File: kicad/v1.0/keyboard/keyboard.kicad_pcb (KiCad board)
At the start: 2 copper layers, 162 x 50 mm, 89 parts, among them J1 PMOD, J2 Conn_01x02, J3 Conn_01x02, SW1 @, SW10 I, SW11 J, SW12 K, SW13 L, SW14 M, SW15 N, SW16 O, SW17 P, SW18 Q, SW19 R, SW2 A, SW20 S, SW21 T, SW22 U, SW23 V, SW24 W, SW25 X, SW26 Y, SW27 Z, SW28 0, SW29 1, SW3 B, SW30 2, SW31 3, SW32 4, SW33 5, SW34 6, SW35 7, SW36 0, SW37 1, SW38 2, SW39 3, SW4 C, SW40 4, SW41 5, SW42 6, SW43 7, SW44 8, SW45 9, SW46 ., SW47 8, SW48 9, SW49 :, SW5 D, SW50 ;, SW51 ,, SW52 -, SW53 ., SW54 /, SW55 ENTER, SW56 ENTER, SW57 CLEAR, SW58 BREAK, SW59 UP, SW6 E, SW60 DOWN, SW61 LEFT, SW62 RIGHT, SW63 SPACE, SW64 RESET, SW65 RSHIFT, SW66 LSHIFT, SW67 SPACE, SW68 SPACE, SW69 ENTER, SW7 F, SW8 G, SW9 H, U1 74LS07, U2 74LS138, U3 74LS07, U4 74LS157

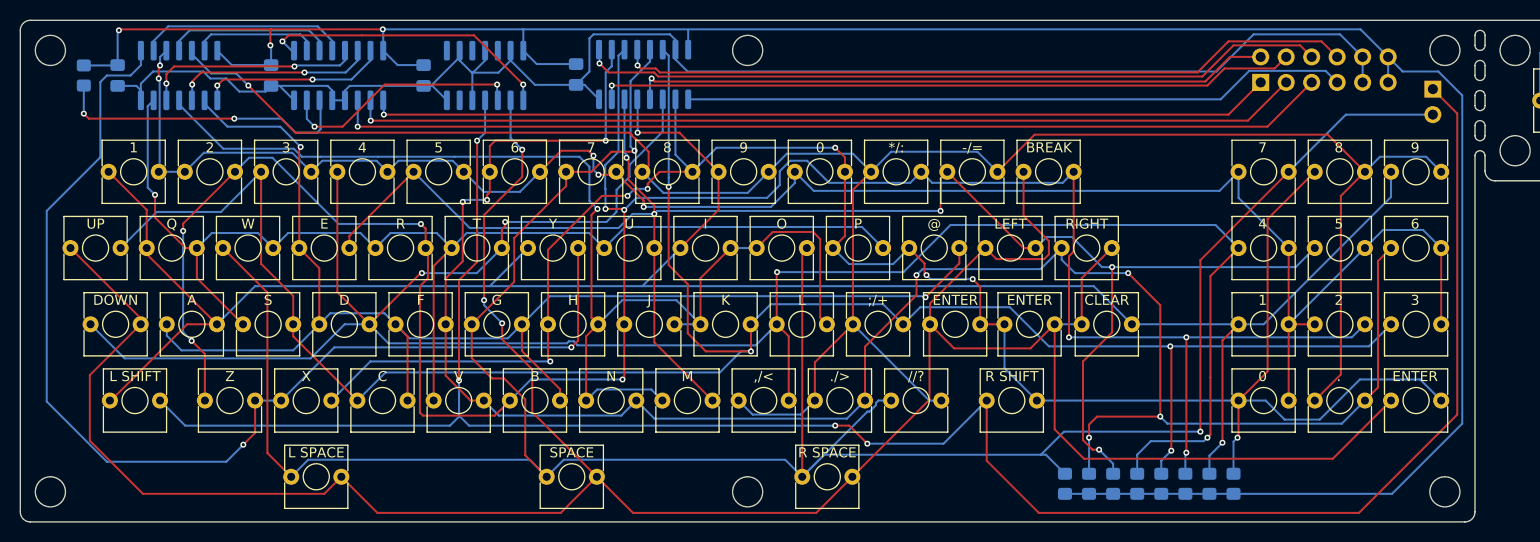
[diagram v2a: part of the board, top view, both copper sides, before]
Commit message: Add ground pour (maboytim)
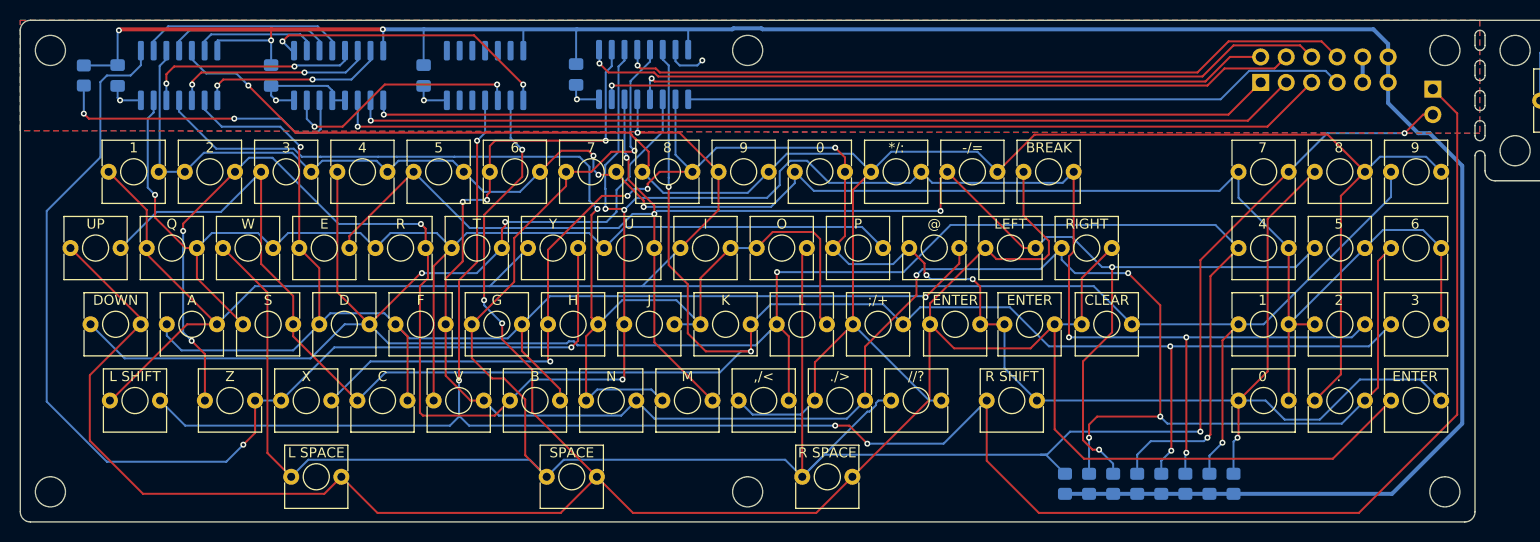
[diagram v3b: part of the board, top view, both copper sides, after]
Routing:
- net GND: track 162.6 -> 29.8 mm, vias 0 -> 5
- net +3.3V: track 247.6 -> 241.3 mm
- net Net-(SW28-Pad2): track 188.5 -> 188.4 mm, vias 5 -> 3
- net Net-(J2-Pin_2): vias 2 -> 3
- added copper zone on B.Cu, net GND
- added copper zone on F.Cu, net GND

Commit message: Add schematics for interface PCB
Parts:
- added D1: LED_RKBG, LED_THT:LED_D5.0mm-4_RGB, F.Cu at (231.9, 153.9)
- added J10: Cassette Input, Library:Jack_3.5mm_CUI_SJ1-3535NG_Horizontal_CircularHoles, F.Cu at (224.8, 146.7)
- added J4: Conn_01x16, Connector_PinHeader_2.54mm:PinHeader_1x16_P2.54mm_Vertical, F.Cu at (207.0, 142.8)
- added J5: Programmer, Connector_PinHeader_2.54mm:PinHeader_1x03_P2.54mm_Horizontal, F.Cu at (232.4, 142.8)
- added J9: SD_Card, Library:TFP09-2-12B, F.Cu at (228.7, 172.4)
- added R16: 10K, Resistor_SMD:R_0805_2012Metric_Pad1.20x1.40mm_HandSolder, F.Cu at (239.9, 151.7)
- added R18: 10K, Resistor_SMD:R_0805_2012Metric_Pad1.20x1.40mm_HandSolder, F.Cu at (239.9, 154.6)
- added SW70: ESP_RESET, Button_Switch_THT:SW_PUSH_6mm, F.Cu at (211.3, 142.5)
- added SW71: PTRS_RESET, Button_Switch_THT:SW_PUSH_6mm, F.Cu at (211.3, 151.1)
- added SW72: TRS_IO_STATUS, Button_Switch_THT:SW_PUSH_6mm, F.Cu at (211.3, 159.6)

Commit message: Updated Interface board
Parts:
- added J11: Cassette Output, Connector_Audio:Jack_3.5mm_CUI_SJ1-3525N_Horizontal, F.Cu at (77.6, 140.0)
- added J12: SD_Card, Library:TFP09-2-12B, F.Cu at (117.6, 139.8)
- J10: footprint Library:Jack_3.5mm_CUI_SJ1-3535NG_Horizontal_CircularHoles -> Connector_Audio:Jack_3.5mm_CUI_SJ1-3525N_Horizontal
- J4: value Conn_01x16 -> Interface Connector; footprint Connector_PinHeader_2.54mm:PinHeader_1x16_P2.54mm_Vertical -> Connector_PinHeader_1.27mm:PinHeader_2x10_P1.27mm_Vertical
- SW70, SW71, SW72: footprint Button_Switch_THT:SW_PUSH_6mm -> Button_Switch_THT:SW_Tactile_SPST_Angled_PTS645Vx83-2LFS
- moved R18 140.3 mm to (101.3, 133.3), turned to -90 degrees
- moved R16 135.3 mm to (105.9, 133.3), turned to -90 degrees
- moved J10 133.7 mm to (91.3, 139.9)
- moved D1 130.8 mm to (101.7, 141.4)
- moved J9 103.6 mm to (134.3, 129.4), turned to 180 degrees
- moved SW72 63.5 mm to (150.4, 141.9), turned to 180 degrees
- moved SW64 53.8 mm to (206.3, 132.5)
- moved J3 53.8 mm to (207.6, 126.5)
- moved SW71 50.8 mm to (161.4, 141.9), turned to 180 degrees
- moved J5 49.4 mm to (183.7, 134.2), turned to -90 degrees
- moved J4 44.7 mm to (164.2, 129.8), turned to -90 degrees
- moved SW70 38.9 mm to (172.4, 141.9), turned to 180 degrees
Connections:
- J10 pad R: IF_CASS_IN -> unconnected-(J10-PadR)
- J10 pad RN: (no net) -> unconnected-(J10-PadRN)
- J10 pad T: unconnected-(J10-PadT) -> IF_CASS_IN
- J10 pad TN: (no net) -> unconnected-(J10-PadTN)
- J4 pad 1: GND -> IF_CASS_OUT
- J4 pad 10: IF_BTN__ESP_RST -> IF_BTN_PTRS_RST
- J4 pad 11: IF_CASS_IN -> IF_SD_MISO
- J4 pad 12: IF_LED_RED -> IF_BTN_TRSIO_STATUS
- J4 pad 13: IF_LED_BLUE -> IF_SD_SCK
- J4 pad 14: IF_LED_GREEN -> IF_SD_CS
- J4 pad 15: IF_RXD0 -> IF_SD_CD
- J4 pad 16: IF_TXD0 -> IF_SD_MOSI
- J4 pad 2: +3V3 -> GND
- J4 pad 3: IF_SD_MISO -> IF_LED_RED
- J4 pad 4: IF_SD_SCK -> IF_TXD0
- J4 pad 5: IF_SD_CD -> IF_LED_BLUE
- J4 pad 6: IF_SD_MOSI -> IF_RXD0
- J4 pad 7: IF_SD_CS -> IF_LED_GREEN
- J4 pad 8: IF_BTN_TRSIO_STATUS -> IF_CASS_IN
- J4 pad 9: IF_BTN_PTRS_RST -> IF_BTN__ESP_RST
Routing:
- net GND: track 29.8 -> 469.1 mm, vias 5 -> 15
- net IF_CASS_OUT: track 0.00 -> 115.3 mm
- net IF_LED_BLUE: track 0.00 -> 100.3 mm
- net IF_LED_RED: track 0.00 -> 100.3 mm
- net IF_LED_GREEN: track 0.00 -> 96.7 mm
- net +3V3: track 0.00 -> 78.5 mm, vias 0 -> 2
- net IF_SD_MOSI: track 0.00 -> 74.4 mm
- net IF_CASS_IN: track 0.00 -> 74.2 mm
- net IF_SD_CS: track 0.00 -> 71.3 mm
- net IF_SD_CD: track 0.00 -> 69.3 mm, vias 0 -> 1
- net IF_SD_MISO: track 0.00 -> 67.8 mm, vias 0 -> 1
- net IF_SD_SCK: track 0.00 -> 62.4 mm, vias 0 -> 1
- net Net-(J12-DAT1): track 0.00 -> 54.0 mm, vias 0 -> 2
- net Net-(J12-DAT2): track 0.00 -> 50.6 mm, vias 0 -> 2
- net IF_BTN__ESP_RST: track 0.00 -> 30.3 mm
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- added copper zone on F.Cu, net +3V3
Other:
- board size 162 x 50 mm -> 145 x 71.6 mm
- board text added: "Cass Input"
- board text added: "Cass Output"
- board text added: "ESP Reset"
- board text added: "GND"
- board text added: "Interface"
- board text added: "Keyboard"
- board text added: "MiniTRS"
- board text added: "PTRS Reset"
- board text added: "Programmer"
- board text added: "RX"
- board text added: "Reset"
- board text added: "Rev 1.1"
- board text added: "SD-Card"
- board text added: "Status"
- board text added: "TX"

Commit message: Update keyboard.kicad_pcb
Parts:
- moved J11 0.05 mm to (77.6, 139.9)
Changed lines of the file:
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@@
 	(footprint "Connector_Audio:Jack_3.5mm_CUI_SJ1-3525N_Horizontal"
 		(layer "F.Cu")
-		(at 77.6 140)
+		(at 77.6 139.95)
 		(descr "TRS 3.5mm, horizontal, through-hole, https://www.cuidevices.com/product/resource/pdf/sj1-352xn.pdf")
 		(tags "TRS audio jack stereo horizontal")
@@
 	)
 	(segment
+		(start 77.6 139.95)
+		(end 77.6 137.4)
+		(width 0.5)
+		(layer "F.Cu")
+		(net 3)
+	)
+	(segment
 		(start 180.9 137.3)
 		(end 185.1 137.3)
@@
 	)
 	(segment
-		(start 77.6 137.4)
-		(end 78.849 136.151)
-		(width 0.5)
-		(layer "F.Cu")
-		(net 3)
-	)
-	(segment
 		(start 83.2 124.502)
 		(end 83.949 125.251)
@@
 	)
 	(segment
-		(start 78.849 136.151)
-		(end 78.849 130.351)
-		(width 0.5)
-		(layer "F.Cu")
-		(net 3)
-	)
-	(segment
 		(start 109.85 137.75)
 		(end 109.9 137.7)
@@
 	)
 	(segment
+		(start 78.75 136.25)
+		(end 78.75 130.45)
+		(width 0.5)
+		(layer "F.Cu")
+		(net 3)
+	)
+	(segment
 		(start 137.6 143.8)
 		(end 143.95 143.8)
@@
 	)
 	(segment
-		(start 78.849 130.351)
-		(end 83.949 125.251)
-		(width 0.5)
-		(layer "F.Cu")
-		(net 3)
-	)
-	(segment
 		(start 110.2 127.1)
 		(end 114 127.1)
@@
 	)
 	(segment
-		(start 77.6 140)
-		(end 77.6 137.4)
-		(width 0.5)
-		(layer "F.Cu")
-		(net 3)
-	)
-	(segment
 		(start 78.84 81.1)
 		(end 72.7 81.1)
@@
 	)
 	(segment
+		(start 77.6 137.4)
+		(end 78.75 136.25)
+		(width 0.5)
+		(layer "F.Cu")
+		(net 3)
+	)
+	(segment
 		(start 169.71 143.7)
 		(end 176 143.7)
@@
 	)
 	(segment
+		(start 78.75 130.45)
+		(end 83.949 125.251)
+		(width 0.5)
+		(layer "F.Cu")
+		(net 3)
+	)
+	(segment
 		(start 137.6 143.8)
 		(end 128.4 143.8)
@@
 	)
 	(segment
+		(start 78.8 141.2)
+		(end 90.1 141.2)
+		(width 0.5)
+		(layer "B.Cu")
+		(net 3)
+	)
+	(segment
 		(start 114.33 80.500001)
 		(end 113.867499 80.0375)
@@
 	)
 	(segment
-		(start 90.1 141.2)
-		(end 91.35 139.95)
-		(width 0.5)
-		(layer "B.Cu")
-		(net 3)
-	)
-	(segment
 		(start 109.47 80.0375)
 		(end 109.47 81.47)
@@
 	)
 	(segment
+		(start 90.1 141.2)
+		(end 91.35 139.95)
+		(width 0.5)
+		(layer "B.Cu")
+		(net 3)
+	)
+	(segment
 		(start 78.97 81.23)
 		(end 78.97 80.0375)
@@
 	)
 	(segment
-		(start 78.8 141.2)
-		(end 90.1 141.2)
+		(start 77.6 139.95)
+		(end 77.6 140)
 		(width 0.5)
 		(layer "B.Cu")
@@
 	)
 	(segment
-		(start 77.6 140)
-		(end 78.8 141.2)
-		(width 0.5)
-		(layer "B.Cu")
-		(net 3)
-	)
-	(segment
 		(start 113.062499 80.0375)
 		(end 111.8 80.0375)
@@
 		(layer "B.Cu")
 		(net 3)
+	)
+	(segment
+		(start 77.6 140)
+		(end 78.8 141.2)
+		(width 0.5)
+		(layer "B.Cu")
+		(net 3)

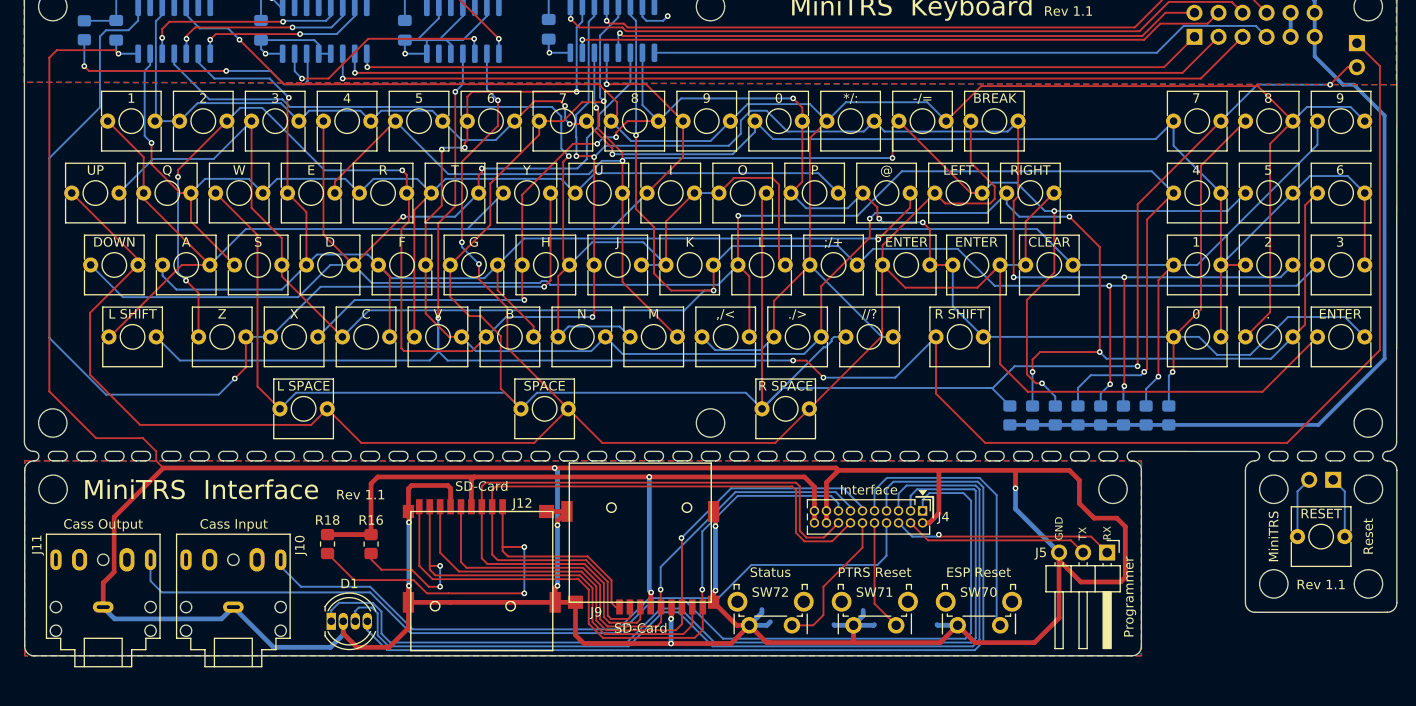
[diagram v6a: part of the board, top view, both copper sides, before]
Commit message: Interface board with Barrel Jack for power
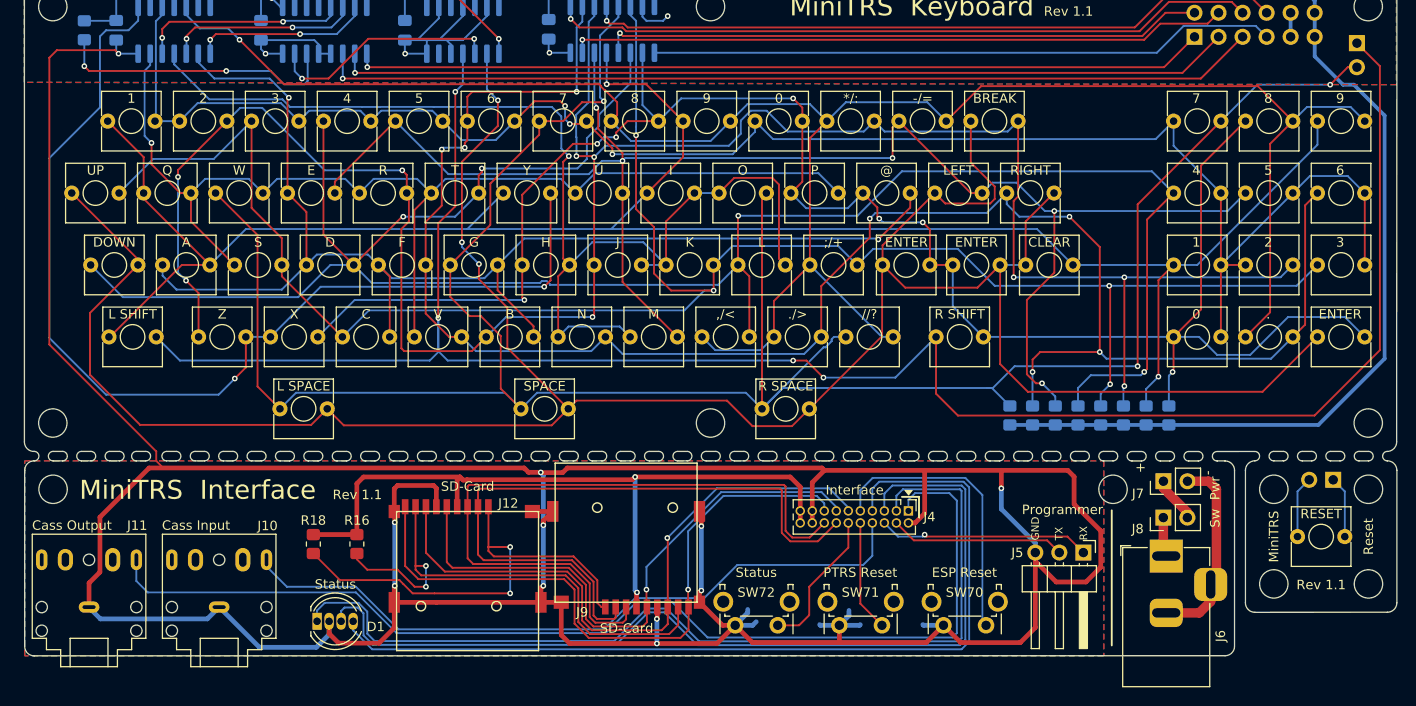
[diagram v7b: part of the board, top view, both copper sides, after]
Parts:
- added J6: Barrel_Jack_Switch, Connector_BarrelJack:BarrelJack_Horizontal, F.Cu at (189.9, 134.6)
- added J7: Pwr Supply, Connector_PinHeader_2.54mm:PinHeader_1x02_P2.54mm_Vertical, F.Cu at (189.6, 126.7)
- added J8: Pwr Switch, Connector_PinHeader_2.54mm:PinHeader_1x02_P2.54mm_Vertical, F.Cu at (189.6, 130.5)
- moved J5 2.51 mm to (181.2, 134.2)
- moved D1 1.50 mm to (100.2, 141.4)
- moved J10 1.50 mm to (89.8, 139.9)
- moved J11 1.50 mm to (76.1, 139.9)
- moved J12 1.50 mm to (116.1, 139.8)
- moved J4 1.50 mm to (162.7, 129.8)
- moved J9 1.50 mm to (132.8, 129.4)
- moved R16 1.50 mm to (104.4, 133.3)
- moved R18 1.50 mm to (99.8, 133.3)
- moved SW70 1.50 mm to (170.9, 141.9)
- moved SW71 1.50 mm to (159.9, 141.9)
- moved SW72 1.50 mm to (148.9, 141.9)
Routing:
- net Net-(J7-Pin_2): track 0.00 -> 20.7 mm
- net GND: track 469.1 -> 463.1 mm
- net Net-(J7-Pin_1): track 0.00 -> 4.89 mm
- net Net-(J8-Pin_1): track 0.00 -> 4.20 mm
- net Net-(J2-Pin_1): track 215.4 -> 213.0 mm
- net Net-(SW55-Pad1): track 271.4 -> 269.1 mm
- net IF_RXD0: track 23.5 -> 22.5 mm
- net IF_TXD0: track 19.5 -> 18.5 mm
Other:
- outline, holes or cut-outs redrawn
- board text added: "+"
- board text added: "-"
- board text added: "Pwr"
- board text added: "Sw"
